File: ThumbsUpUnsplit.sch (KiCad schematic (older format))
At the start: 68 parts, among them J2 Conn_01x04_Female, J3 Conn_01x04_Female, J4 Conn_01x04_Female, SW1 SW_Push, U1 ATmega32U4-AU, Y1 16MHz

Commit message: Laid out the matrix
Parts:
- removed D10, D11, D12, D13, D14, D15, D16, D17, D18, D19, D20, D21, D22, D4, D8, D9: D_Small, Diode_SMD:D_SOD-123, symbol Device:D_Small
- removed J2, J3, J4: Conn_01x04_Female, Connector_PinHeader_2.54mm:PinHeader_1x04_P2.54mm_Vertical, symbol Connector:Conn_01x04_Female
- removed MX10, MX11, MX12, MX13, MX14, MX15, MX16, MX17, MX18, MX19, MX20, MX21, MX22, MX4, MX8, MX9: MX-NoLED, MX_Alps_Hybrid:MX-Alps-Choc-X-1U-NoLED, symbol MX_Alps_Hybrid:MX-NoLED
- removed R5: 10k, Resistor_SMD:R_0805_2012Metric, symbol Device:R_Small
- removed Right-Left1: JP1, Jumper:SolderJumper-3_P1.3mm_Open_Pad1.0x1.5mm, symbol Jumper:SolderJumper_3_Open
- added D? (x38): D_Small, Diode_SMD:D_SOD-123, symbol Device:D_Small
- added J? (x2): Conn_01x18_Female, symbol Connector:Conn_01x18_Female
- added J? (x2): Conn_01x18_Male, symbol Connector:Conn_01x18_Male
- added J? (x2): Conn_01x04_Female, symbol Connector:Conn_01x04_Female
- added J? (x2): Conn_01x04_Male, symbol Connector:Conn_01x04_Male
- added MX? (x38): MX-NoLED, MX_Alps_Hybrid:MX-Alps-Choc-X-1U-NoLED, symbol MX_Alps_Hybrid:MX-NoLED
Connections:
- net COL0: now also J?.1 (Pin_1)
- net COL1: now also J?.2 (Pin_2)
- net COL2: now also J?.3 (Pin_3)
- net COL3: now also J?.4 (Pin_4)
- net COL4: now also J?.1 (Pin_1)
- net COL5: now also J?.4 (Pin_4)
- net ROW0: now also D?.1 (K), D?.1 (K), D?.1 (K), D?.1 (K), D?.1 (K), D?.1 (K), D?.1 (K), D?.1 (K), D?.1 (K), D?.1 (K)
- net ROW1: now also D?.1 (K), D?.1 (K), D?.1 (K), D?.1 (K), D?.1 (K), D?.1 (K), D?.1 (K), D?.1 (K), D?.1 (K), D?.1 (K)
- net ROW2: now also D?.1 (K), D?.1 (K), D?.1 (K), D?.1 (K), D?.1 (K), D?.1 (K), D?.1 (K), D?.1 (K), D?.1 (K), D?.1 (K)
- net ROW3: now also D?.1 (K), D?.1 (K), D?.1 (K), D?.1 (K), D?.1 (K), D?.1 (K), D?.1 (K), D?.1 (K)
- new net: J?.1 (Pin_1), MX?.1 (COL), MX?.1 (COL), MX?.1 (COL) (x2)
- new net: J?.8 (Pin_8), MX?.2 (ROW) (x2)
- new net: J?.2 (Pin_2), MX?.1 (COL), MX?.1 (COL), MX?.1 (COL) (x2)
- new net: J?.7 (Pin_7), MX?.2 (ROW) (x2)
- new net: J?.12 (Pin_12), MX?.2 (ROW) (x2)
- new net: J?.11 (Pin_11), MX?.2 (ROW) (x2)
- new net: J?.3 (Pin_3), MX?.1 (COL), MX?.1 (COL), MX?.1 (COL), MX?.1 (COL) (x2)
- new net: J?.6 (Pin_6), MX?.2 (ROW) (x2)
- new net: J?.4 (Pin_4), MX?.1 (COL), MX?.1 (COL), MX?.1 (COL), MX?.1 (COL) (x2)
- new net: J?.5 (Pin_5), MX?.2 (ROW) (x2)
- new net: J?.10 (Pin_10), MX?.2 (ROW) (x2)
- new net: J?.9 (Pin_9), MX?.2 (ROW) (x2)
- new net: J?.16 (Pin_16), MX?.2 (ROW) (x2)
- new net: J?.15 (Pin_15), MX?.2 (ROW) (x2)
- new net: J?.14 (Pin_14), MX?.2 (ROW) (x2)
- new net: J?.13 (Pin_13), MX?.2 (ROW) (x2)
- new net: J?.18 (Pin_18), MX?.2 (ROW) (x2)
- new net: J?.17 (Pin_17), MX?.2 (ROW) (x2)
- new net: D?.2 (A), MX?.2 (ROW) (x6)
- new net: D?.2 (A), J?.10 (Pin_10) (x2)
- new net: D?.2 (A), J?.11 (Pin_11) (x2)
- new net: D?.2 (A), J?.12 (Pin_12) (x2)
- new net: D?.2 (A), J?.13 (Pin_13) (x2)
- new net: D?.2 (A), J?.14 (Pin_14) (x2)
- new net: D?.2 (A), J?.15 (Pin_15) (x2)
- new net: D?.2 (A), J?.16 (Pin_16) (x2)
- new net: D?.2 (A), J?.17 (Pin_17) (x2)
- new net: D?.2 (A), J?.18 (Pin_18) (x2)
- new net: D?.2 (A), J?.5 (Pin_5) (x2)
- new net: D?.2 (A), J?.6 (Pin_6) (x2)
- new net: D?.2 (A), J?.7 (Pin_7) (x2)
- new net: D?.2 (A), J?.8 (Pin_8) (x2)
- new net: D?.2 (A), J?.9 (Pin_9) (x2)
- new net: D?.2 (A), J?.3 (Pin_3) (x2)
- new net: D?.2 (A), J?.2 (Pin_2) (x2)
- new net: J?.1 (Pin_1), MX?.1 (COL) (x2)
- new net: J?.2 (Pin_2), MX?.2 (ROW) (x2)
- new net: J?.4 (Pin_4), MX?.1 (COL) (x2)
- new net: J?.3 (Pin_3), MX?.2 (ROW) (x2)
- new net COL6: J?.1 (Pin_1), MX?.1 (COL), MX?.1 (COL), MX?.1 (COL)
- new net COL7: J?.4 (Pin_4), MX?.1 (COL), MX?.1 (COL), MX?.1 (COL)
- new net COL8: J?.4 (Pin_4)
- new net COL9: J?.3 (Pin_3)
- new net COLA: J?.2 (Pin_2)
- new net COLB: J?.1 (Pin_1)
- no-connect marks 10 -> 5
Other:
- moved on the sheet: D1, D2, D3, D5, D6, D7, F1, MX1, MX2, MX3, MX5, MX6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

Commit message: Layed out the switches and edge cuts
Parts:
- J1, J8: renamed from J?; footprint (none) -> Connector_PinHeader_2.54mm:PinHeader_1x18_P2.54mm_Vertical
- J2, J7: renamed from J?; footprint (none) -> Connector_PinSocket_2.54mm:PinSocket_1x18_P2.54mm_Vertical
- J3, J5: renamed from J?; footprint (none) -> Connector_PinSocket_2.54mm:PinSocket_1x04_P2.54mm_Vertical
- J4, J6: renamed from J?; footprint (none) -> Connector_PinHeader_2.54mm:PinHeader_1x04_P2.54mm_Vertical
- MX1, MX10, MX11, MX12, MX13, MX14, MX15, MX16, MX17, MX18, MX19, MX2, MX20, MX21, MX22, MX26, MX3, MX30, MX31, MX32, MX33, MX34, MX35, MX36, MX37, MX38, MX39, MX4, MX40, MX41, MX42, MX43, MX44, MX5, MX6, MX7, MX8, MX9: renamed from MX?; footprint MX_Alps_Hybrid:MX-Alps-Choc-X-1U-NoLED -> SwitchFootprints:MX-Alps-Choc-KS32-X-1U-NoLED
- MX23: renamed from MX1; footprint MX_Alps_Hybrid:MX-Alps-Choc-X-1U-NoLED -> SwitchFootprints:MX-Alps-Choc-KS32-X-1U-NoLED
- MX24: renamed from MX2; footprint MX_Alps_Hybrid:MX-Alps-Choc-X-1U-NoLED -> SwitchFootprints:MX-Alps-Choc-KS32-X-1U-NoLED
- MX25: renamed from MX3; footprint MX_Alps_Hybrid:MX-Alps-Choc-X-1U-NoLED -> SwitchFootprints:MX-Alps-Choc-KS32-X-1U-NoLED
- MX27: renamed from MX5; footprint MX_Alps_Hybrid:MX-Alps-Choc-X-1U-NoLED -> SwitchFootprints:MX-Alps-Choc-KS32-X-1U-NoLED
- MX28: renamed from MX6; footprint MX_Alps_Hybrid:MX-Alps-Choc-X-1U-NoLED -> SwitchFootprints:MX-Alps-Choc-KS32-X-1U-NoLED
- MX29: renamed from MX7; footprint MX_Alps_Hybrid:MX-Alps-Choc-X-1U-NoLED -> SwitchFootprints:MX-Alps-Choc-KS32-X-1U-NoLED
- gave numbers to parts that had none: 38
- renumbered C8 to C1, C11 to C10, C1 to C2, C9 to C3, C2 to C4, C3 to C5, C4 to C6, C5 to C7, C6 to C8, C7 to C9, D1 to D23, D2 to D24, D3 to D25, D5 to D26, D6 to D27, D7 to D28
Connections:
- net SCL is gone; now on net ROW0: U1.18 (PD0)
- net COL0: now also U1.40 (PF1); no longer U1.37 (PF6)
- net COL1: now also U1.41 (PF0); no longer U1.36 (PF7)
- net COL2: now also U1.8 (PB0); no longer U1.9 (PB1)
- net COL3: now also U1.32 (PC7); no longer U1.11 (PB3)
- net COL4: now also U1.39 (PF4); no longer U1.10 (PB2)
- net COL5: now also U1.38 (PF5); no longer U1.30 (PB6)
- net COL6: now also U1.37 (PF6)
- net COL7: now also U1.36 (PF7)
- net COL8: now also U1.25 (PD4)
- net COL9: now also U1.26 (PD6)
- net COLA: now also U1.28 (PB4)
- net COLB: now also U1.27 (PD7)
- net ROW0: no longer U1.27 (PD7)
- net ROW1: now also U1.22 (PD5); no longer U1.1 (PE6)
- net ROW2: now also U1.29 (PB5); no longer U1.28 (PB4)
- net ROW3: now also U1.30 (PB6); no longer U1.29 (PB5)
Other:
- note added: "As in Planck/rev4:\n\n#define MATRIX_ROW_PINS { D0, D5, B5, B6 }\n#define MATRIX_COL_PINS { F1, F0, B0, C7, F4, F5, F6, F7, D4, D6, B4, D7 }\n\n#define DIODE_DIRECTION COL2ROW\n"

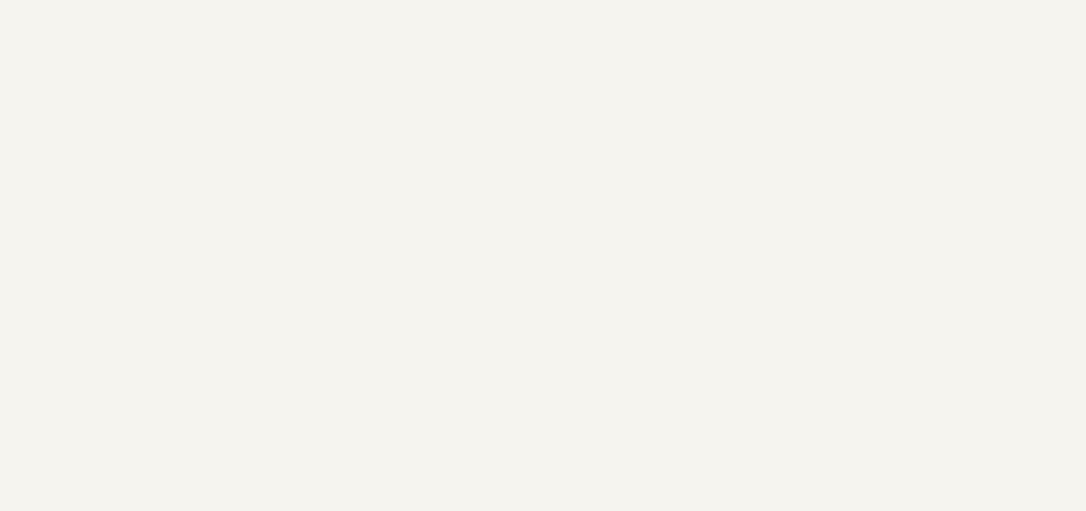
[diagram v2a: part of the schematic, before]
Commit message: Roughed in the connectors
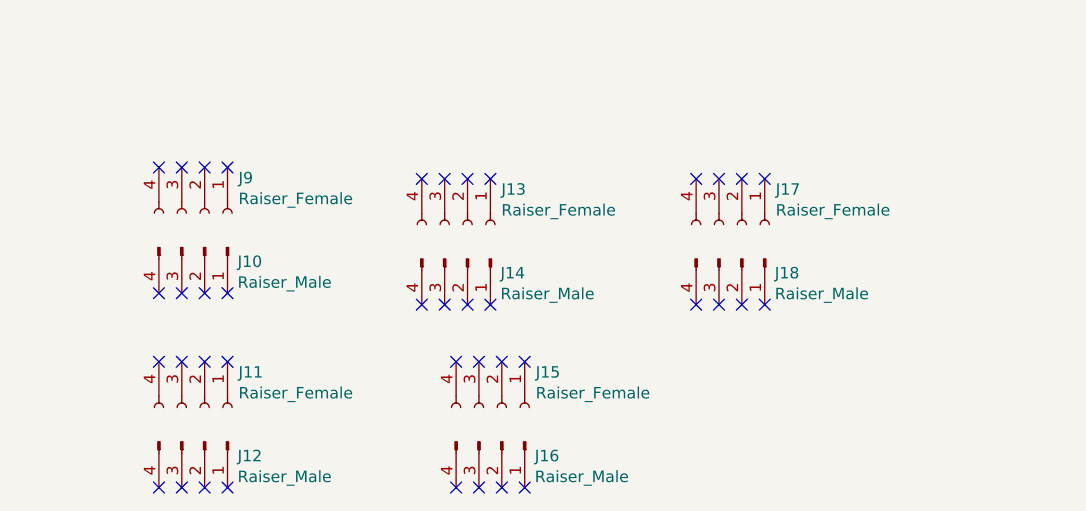
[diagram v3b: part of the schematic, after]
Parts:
- added J10, J12, J14, J16, J18: Raiser_Male, Connector_PinHeader_2.54mm:PinHeader_1x04_P2.54mm_Vertical, symbol Connector:Conn_01x04_Male
- added J11, J13, J15, J17, J9: Raiser_Female, Connector_PinSocket_2.54mm:PinSocket_1x04_P2.54mm_Vertical, symbol Connector:Conn_01x04_Female
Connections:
- no-connect marks 5 -> 45
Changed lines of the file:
@@
 Text GLabel 4200 4150 2    50   Input ~ 0
 COLB
+$Comp
+L Connector:Conn_01x04_Female J11
+U 1 1 6206CD49
+P 1750 12400
+F 0 "J11" V 1596 12548 50  0000 L CNN
+F 1 "Raiser_Female" V 1687 12548 50  0000 L CNN
+F 2 "Connector_PinSocket_2.54mm:PinSocket_1x04_P2.54mm_Vertical" H 1750 12400 50  0001 C CNN
+F 3 "~" H 1750 12400 50  0001 C CNN
+	1    1750 12400
+	0    1    1    0
+$EndComp
+$Comp
+L Connector:Conn_01x04_Male J12
+U 1 1 6206CD4F
+P 1750 12550
+F 0 "J12" V 1812 12694 50  0000 L CNN
+F 1 "Raiser_Male" V 1903 12694 50  0000 L CNN
+F 2 "Connector_PinHeader_2.54mm:PinHeader_1x04_P2.54mm_Vertical" H 1750 12550 50  0001 C CNN
+F 3 "~" H 1750 12550 50  0001 C CNN
+	1    1750 12550
+	0    1    1    0
+$EndComp
+NoConn ~ 1550 12200
+NoConn ~ 1650 12200
+NoConn ~ 1750 12200
+NoConn ~ 1850 12200
+NoConn ~ 1550 12750
+NoConn ~ 1650 12750
+NoConn ~ 1750 12750
+NoConn ~ 1850 12750
+$Comp
+L Connector:Conn_01x04_Female J9
+U 1 1 621DC2BB
+P 1750 11550
+F 0 "J9" V 1596 11698 50  0000 L CNN
+F 1 "Raiser_Female" V 1687 11698 50  0000 L CNN
+F 2 "Connector_PinSocket_2.54mm:PinSocket_1x04_P2.54mm_Vertical" H 1750 11550 50  0001 C CNN
+F 3 "~" H 1750 11550 50  0001 C CNN
+	1    1750 11550
+	0    1    1    0
+$EndComp
+$Comp
+L Connector:Conn_01x04_Male J10
+U 1 1 621DC2C5
+P 1750 11700
+F 0 "J10" V 1812 11844 50  0000 L CNN
+F 1 "Raiser_Male" V 1903 11844 50  0000 L CNN
+F 2 "Connector_PinHeader_2.54mm:PinHeader_1x04_P2.54mm_Vertical" H 1750 11700 50  0001 C CNN
+F 3 "~" H 1750 11700 50  0001 C CNN
+	1    1750 11700
+	0    1    1    0
+$EndComp
+NoConn ~ 1550 11350
+NoConn ~ 1650 11350
+NoConn ~ 1750 11350
+NoConn ~ 1850 11350
+NoConn ~ 1550 11900
+NoConn ~ 1650 11900
+NoConn ~ 1750 11900
+NoConn ~ 1850 11900
+$Comp
+L Connector:Conn_01x04_Female J13
+U 1 1 62208DC7
+P 2900 11600
+F 0 "J13" V 2746 11748 50  0000 L CNN
+F 1 "Raiser_Female" V 2837 11748 50  0000 L CNN
+F 2 "Connector_PinSocket_2.54mm:PinSocket_1x04_P2.54mm_Vertical" H 2900 11600 50  0001 C CNN
+F 3 "~" H 2900 11600 50  0001 C CNN
+	1    2900 11600
+	0    1    1    0
+$EndComp
+$Comp
+L Connector:Conn_01x04_Male J14
+U 1 1 62208DD1
+P 2900 11750
+F 0 "J14" V 2962 11894 50  0000 L CNN
+F 1 "Raiser_Male" V 3053 11894 50  0000 L CNN
+F 2 "Connector_PinHeader_2.54mm:PinHeader_1x04_P2.54mm_Vertical" H 2900 11750 50  0001 C CNN
+F 3 "~" H 2900 11750 50  0001 C CNN
+	1    2900 11750
+	0    1    1    0
+$EndComp
+NoConn ~ 2700 11400
+NoConn ~ 2800 11400
+NoConn ~ 2900 11400
+NoConn ~ 3000 11400
+NoConn ~ 2700 11950
+NoConn ~ 2800 11950
+NoConn ~ 2900 11950
+NoConn ~ 3000 11950
+$Comp
+L Connector:Conn_01x04_Female J15
+U 1 1 6225ECEC
+P 3050 12400
+F 0 "J15" V 2896 12548 50  0000 L CNN
+F 1 "Raiser_Female" V 2987 12548 50  0000 L CNN
+F 2 "Connector_PinSocket_2.54mm:PinSocket_1x04_P2.54mm_Vertical" H 3050 12400 50  0001 C CNN
+F 3 "~" H 3050 12400 50  0001 C CNN
+	1    3050 12400
+	0    1    1    0
+$EndComp
+$Comp
+L Connector:Conn_01x04_Male J16
+U 1 1 6225ECF6
+P 3050 12550
+F 0 "J16" V 3112 12694 50  0000 L CNN
+F 1 "Raiser_Male" V 3203 12694 50  0000 L CNN
+F 2 "Connector_PinHeader_2.54mm:PinHeader_1x04_P2.54mm_Vertical" H 3050 12550 50  0001 C CNN
+F 3 "~" H 3050 12550 50  0001 C CNN
+	1    3050 12550
+	0    1    1    0
+$EndComp
+NoConn ~ 2850 12200
+NoConn ~ 2950 12200
+NoConn ~ 3050 12200
+NoConn ~ 3150 12200
+NoConn ~ 2850 12750
+NoConn ~ 2950 12750
+NoConn ~ 3050 12750
+NoConn ~ 3150 12750
+$Comp
+L Connector:Conn_01x04_Female J17
+U 1 1 622DE716
+P 4100 11600
+F 0 "J17" V 3946 11748 50  0000 L CNN
+F 1 "Raiser_Female" V 4037 11748 50  0000 L CNN
+F 2 "Connector_PinSocket_2.54mm:PinSocket_1x04_P2.54mm_Vertical" H 4100 11600 50  0001 C CNN
+F 3 "~" H 4100 11600 50  0001 C CNN
+	1    4100 11600
+	0    1    1    0
+$EndComp
+$Comp
+L Connector:Conn_01x04_Male J18
+U 1 1 622DE720
+P 4100 11750
+F 0 "J18" V 4162 11894 50  0000 L CNN
+F 1 "Raiser_Male" V 4253 11894 50  0000 L CNN
+F 2 "Connector_PinHeader_2.54mm:PinHeader_1x04_P2.54mm_Vertical" H 4100 11750 50  0001 C CNN
+F 3 "~" H 4100 11750 50  0001 C CNN
+	1    4100 11750
+	0    1    1    0
+$EndComp
+NoConn ~ 3900 11400
+NoConn ~ 4000 11400
+NoConn ~ 4100 11400
+NoConn ~ 4200 11400
+NoConn ~ 3900 11950
+NoConn ~ 4000 11950
+NoConn ~ 4100 11950
+NoConn ~ 4200 11950
 $EndSCHEMATC

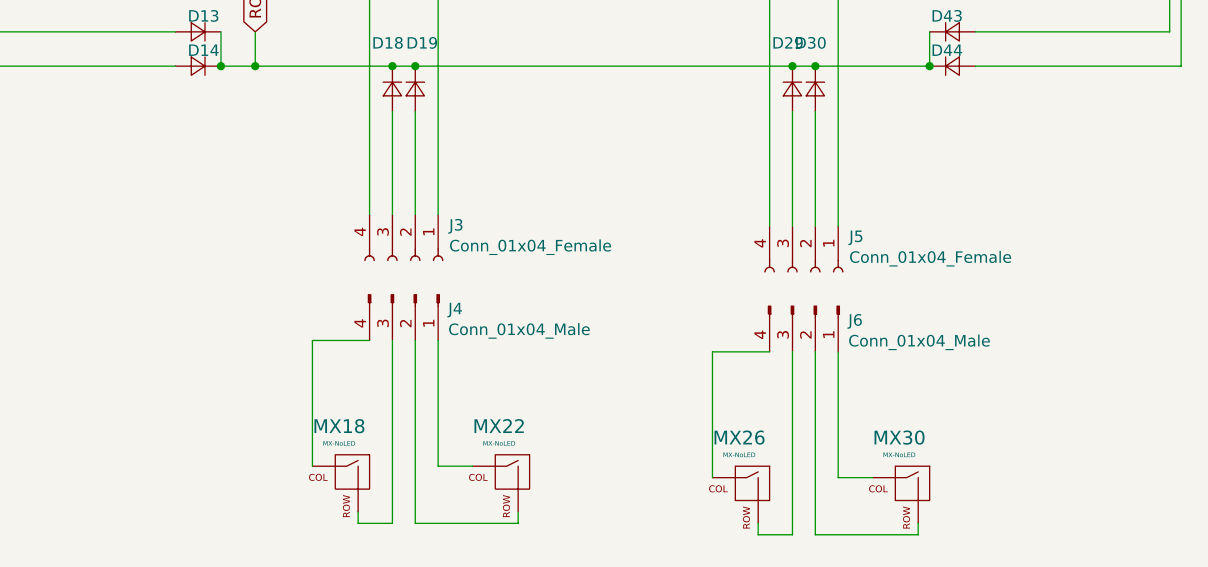
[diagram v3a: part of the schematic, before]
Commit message: Bottom plate routed
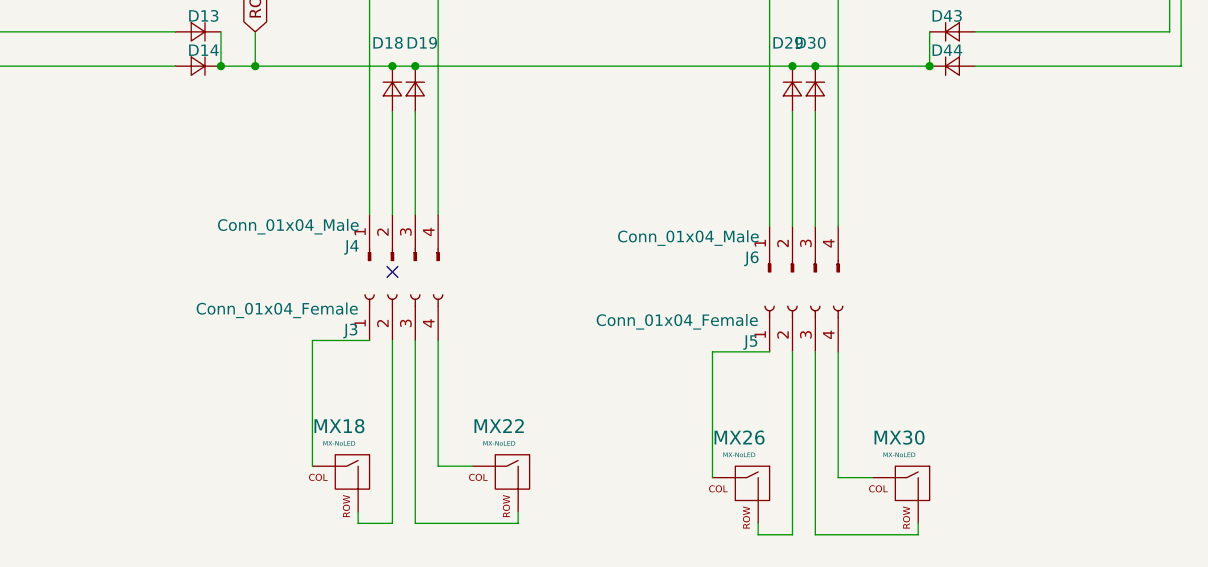
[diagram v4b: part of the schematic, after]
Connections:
- net COL4: now also J6.4 (Pin_4); no longer J5.1 (Pin_1)
- net COL5: now also J6.1 (Pin_1); no longer J5.4 (Pin_4)
- net COL6: now also J4.4 (Pin_4); no longer J3.1 (Pin_1)
- net COL7: now also J4.1 (Pin_1); no longer J3.4 (Pin_4)
- net at D18.2 (A): now also J4.2 (Pin_2); no longer J3.3 (Pin_3)
- net at D19.2 (A): now also J4.3 (Pin_3); no longer J3.2 (Pin_2)
- net at D29.2 (A): now also J6.2 (Pin_2); no longer J5.3 (Pin_3)
- net at D30.2 (A): now also J6.3 (Pin_3); no longer J5.2 (Pin_2)
- net at MX22.1 (COL): now also J3.4 (Pin_4); no longer J4.1 (Pin_1)
- net at MX22.2 (ROW): now also J3.3 (Pin_3); no longer J4.2 (Pin_2)
- net at MX18.1 (COL): now also J3.1 (Pin_1); no longer J4.4 (Pin_4)
- net at MX18.2 (ROW): now also J3.2 (Pin_2); no longer J4.3 (Pin_3)
- net at MX30.1 (COL): now also J5.4 (Pin_4); no longer J6.1 (Pin_1)
- net at MX30.2 (ROW): now also J5.3 (Pin_3); no longer J6.2 (Pin_2)
- net at MX26.1 (COL): now also J5.1 (Pin_1); no longer J6.4 (Pin_4)
- net at MX26.2 (ROW): now also J5.2 (Pin_2); no longer J6.3 (Pin_3)
- no-connect marks 45 -> 46
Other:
- moved on the sheet: J3, J4, J5, J6
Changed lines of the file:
@@
 L Connector:Conn_01x04_Female J3
 U 1 1 628F3D37
-P 8450 10050
-F 0 "J3" V 8296 10198 50  0000 L CNN
-F 1 "Conn_01x04_Female" V 8387 10198 50  0000 L CNN
-F 2 "Connector_PinSocket_2.54mm:PinSocket_1x04_P2.54mm_Vertical" H 8450 10050 50  0001 C CNN
-F 3 "~" H 8450 10050 50  0001 C CNN
-	1    8450 10050
-	0    1    1    0
+P 8350 10200
+F 0 "J3" V 8196 10348 50  0000 L CNN
+F 1 "Conn_01x04_Female" V 8287 10348 50  0000 L CNN
+F 2 "Connector_PinSocket_2.54mm:PinSocket_1x04_P2.54mm_Vertical" H 8350 10200 50  0001 C CNN
+F 3 "~" H 8350 10200 50  0001 C CNN
+	1    8350 10200
+	0    -1   -1   0
 $EndComp
 $Comp
 L Connector:Conn_01x04_Male J4
 U 1 1 628F6492
-P 8450 10200
-F 0 "J4" V 8512 10344 50  0000 L CNN
-F 1 "Conn_01x04_Male" V 8603 10344 50  0000 L CNN
-F 2 "Connector_PinHeader_2.54mm:PinHeader_1x04_P2.54mm_Vertical" H 8450 10200 50  0001 C CNN
-F 3 "~" H 8450 10200 50  0001 C CNN
-	1    8450 10200
-	0    1    1    0
+P 8350 10050
+F 0 "J4" V 8412 10194 50  0000 L CNN
+F 1 "Conn_01x04_Male" V 8503 10194 50  0000 L CNN
+F 2 "Connector_PinHeader_2.54mm:PinHeader_1x04_P2.54mm_Vertical" H 8350 10050 50  0001 C CNN
+F 3 "~" H 8350 10050 50  0001 C CNN
+	1    8350 10050
+	0    -1   -1   0
 $EndComp
 Wire Wire Line
@@
 L Connector:Conn_01x04_Female J5
 U 1 1 62A1D5D4
-P 10200 10100
-F 0 "J5" V 10046 10248 50  0000 L CNN
-F 1 "Conn_01x04_Female" V 10137 10248 50  0000 L CNN
-F 2 "Connector_PinSocket_2.54mm:PinSocket_1x04_P2.54mm_Vertical" H 10200 10100 50  0001 C CNN
-F 3 "~" H 10200 10100 50  0001 C CNN
-	1    10200 10100
-	0    1    1    0
+P 10100 10250
+F 0 "J5" V 9946 10398 50  0000 L CNN
+F 1 "Conn_01x04_Female" V 10037 10398 50  0000 L CNN
+F 2 "Connector_PinSocket_2.54mm:PinSocket_1x04_P2.54mm_Vertical" H 10100 10250 50  0001 C CNN
+F 3 "~" H 10100 10250 50  0001 C CNN
+	1    10100 10250
+	0    -1   -1   0
 $EndComp
 $Comp
 L Connector:Conn_01x04_Male J6
 U 1 1 62A1D5DA
-P 10200 10250
-F 0 "J6" V 10262 10394 50  0000 L CNN
-F 1 "Conn_01x04_Male" V 10353 10394 50  0000 L CNN
-F 2 "Connector_PinHeader_2.54mm:PinHeader_1x04_P2.54mm_Vertical" H 10200 10250 50  0001 C CNN
-F 3 "~" H 10200 10250 50  0001 C CNN
-	1    10200 10250
-	0    1    1    0
+P 10100 10100
+F 0 "J6" V 10162 10244 50  0000 L CNN
+F 1 "Conn_01x04_Male" V 10253 10244 50  0000 L CNN
+F 2 "Connector_PinHeader_2.54mm:PinHeader_1x04_P2.54mm_Vertical" H 10100 10100 50  0001 C CNN
+F 3 "~" H 10100 10100 50  0001 C CNN
+	1    10100 10100
+	0    -1   -1   0
 $EndComp
 Wire Wire Line
@@
 NoConn ~ 4100 11950
 NoConn ~ 4200 11950
+NoConn ~ 8350 10100
 $EndSCHEMATC

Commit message: Left side roughed in
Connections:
- no-connect marks 46 -> 44
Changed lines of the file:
@@
 Wire Wire Line
 	6600 8850 7400 8850
-NoConn ~ 5750 8650
 $Comp
 L Device:D_Small D13
@@
 NoConn ~ 4100 11950
 NoConn ~ 4200 11950
-NoConn ~ 8350 10100
 $EndSCHEMATC
